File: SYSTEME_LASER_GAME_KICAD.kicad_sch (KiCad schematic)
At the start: 4 parts, among them U1 nRF9151-LAXX, U2 LDO_3.3V_0.1A

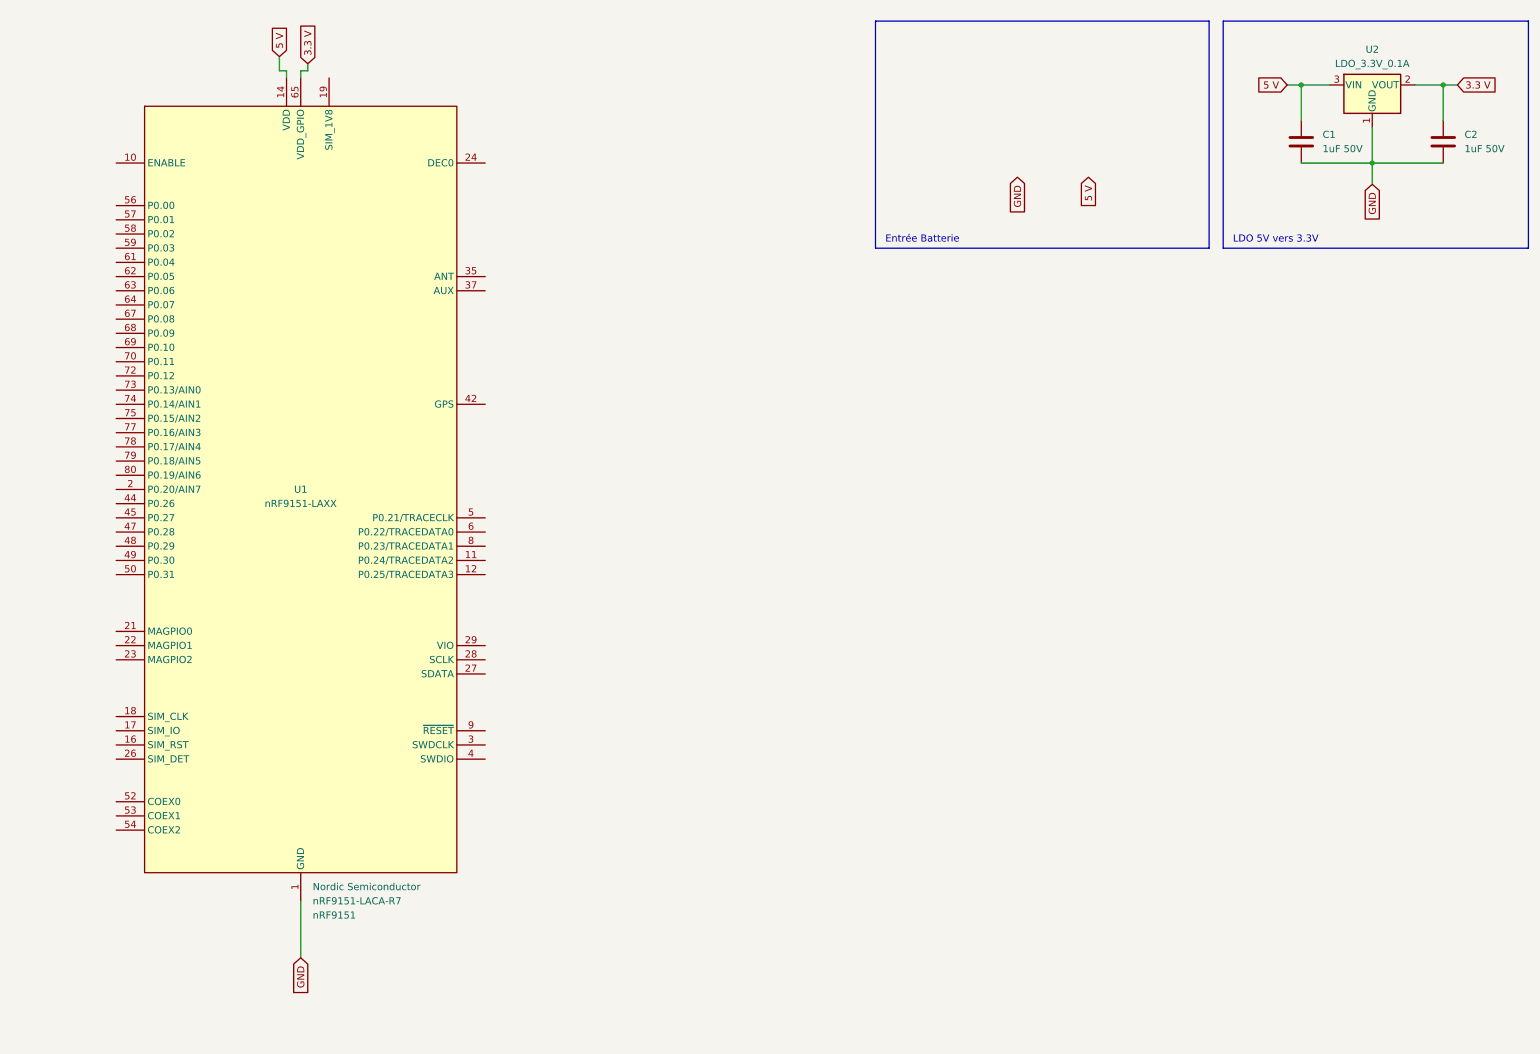
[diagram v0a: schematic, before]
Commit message: réalisation des tests, et fixation des nombres de composants sur le KiCad
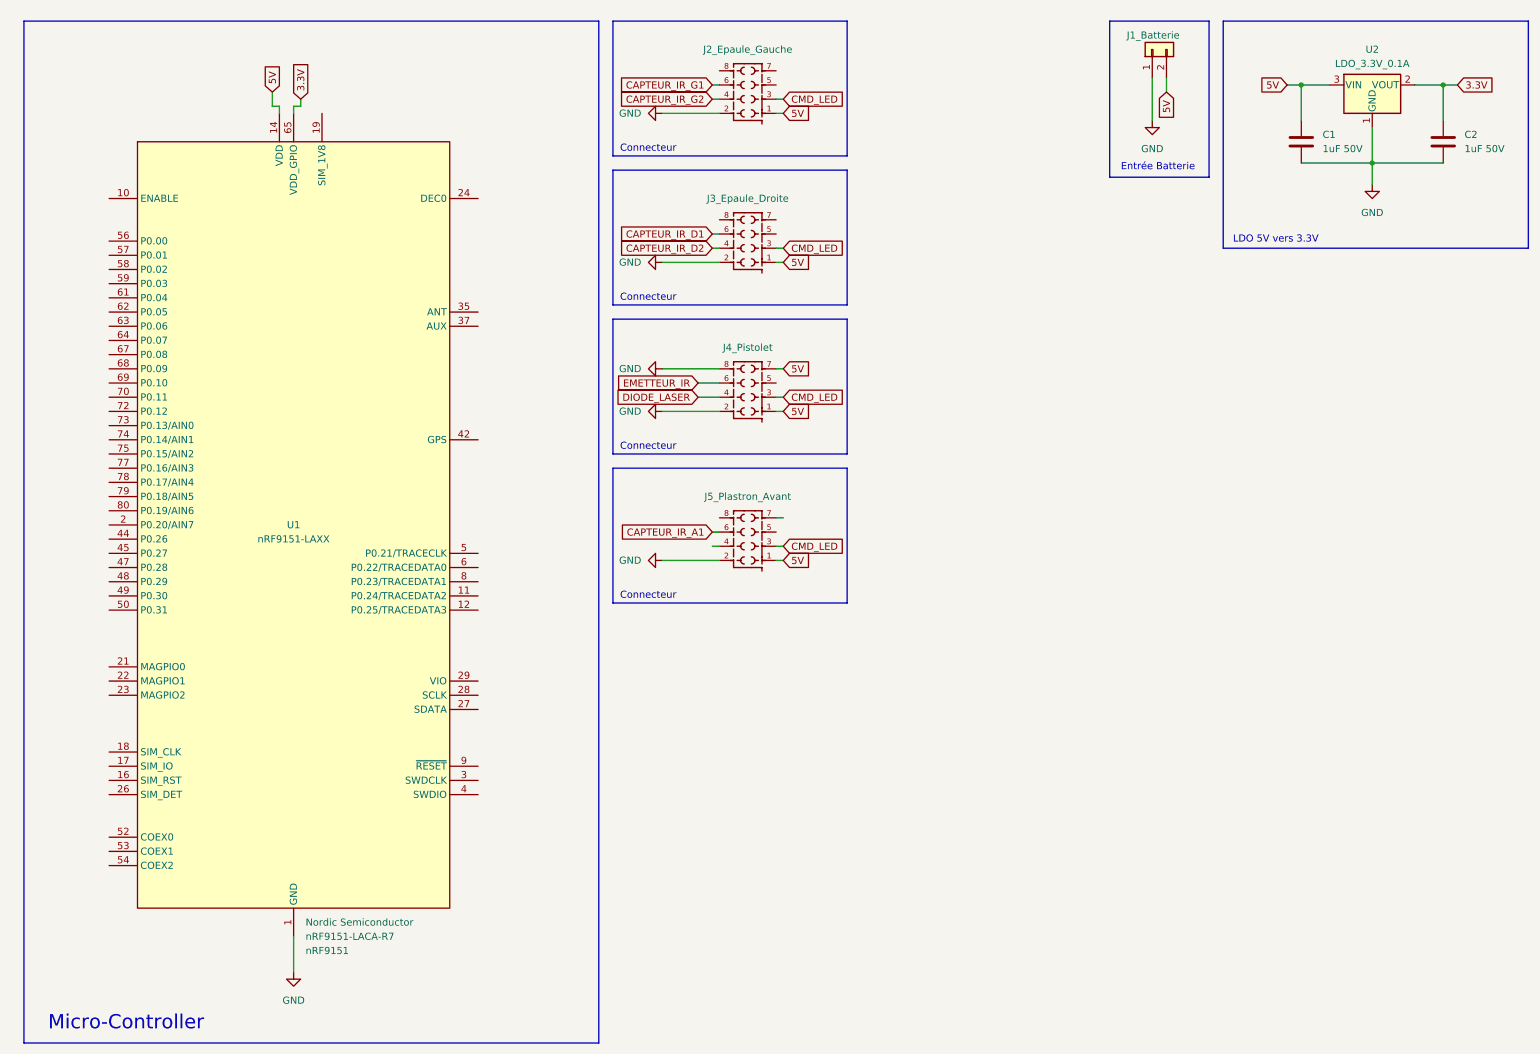
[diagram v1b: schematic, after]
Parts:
- added J1_Batterie: EMB_P3.81_1x02_VERTICAL, codium_Connectors:Conn_THT_3.81_2x1_Vertical, symbol codium_Connectors:EMB_P3.81_1x02_VERTICAL
- added J2_Epaule_Gauche, J3_Epaule_Droite, J4_Pistolet, J5_Plastron_Avant: PinSocket_2x04_P2.54mm_Horizontal_SMD, codium_Connectors:PinSocket_2x04_P2.54mm_Horizontal_SMD, symbol codium_Connectors:PinSocket_2x04_P2.54mm_Horizontal_SMD
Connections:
- net GND: now also J1_Batterie.1 (Pin_1), J2_Epaule_Gauche.2, J3_Epaule_Droite.2, J4_Pistolet.2, J4_Pistolet.8, J5_Plastron_Avant.2
- net 3.3 V renamed 3.3V
- net 5 V renamed 5V
- net 5V: now also J1_Batterie.2 (Pin_2), J2_Epaule_Gauche.1, J3_Epaule_Droite.1, J4_Pistolet.1, J4_Pistolet.7, J5_Plastron_Avant.1
- new net CAPTEUR_IR_A1: J5_Plastron_Avant.6
- new net CAPTEUR_IR_D1: J3_Epaule_Droite.6
- new net CAPTEUR_IR_D2: J3_Epaule_Droite.4
- new net CAPTEUR_IR_G1: J2_Epaule_Gauche.6
- new net CAPTEUR_IR_G2: J2_Epaule_Gauche.4
- new net CMD_LED: J2_Epaule_Gauche.3, J3_Epaule_Droite.3, J4_Pistolet.3, J5_Plastron_Avant.3
- new net DIODE_LASER: J4_Pistolet.4
- new net EMETTEUR_IR: J4_Pistolet.6
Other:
- note added: "Connecteur"
- note added: "Micro-Controller"
- moved on the sheet: U1

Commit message: Finalisation test IR et amélioration CAO sur KiCad
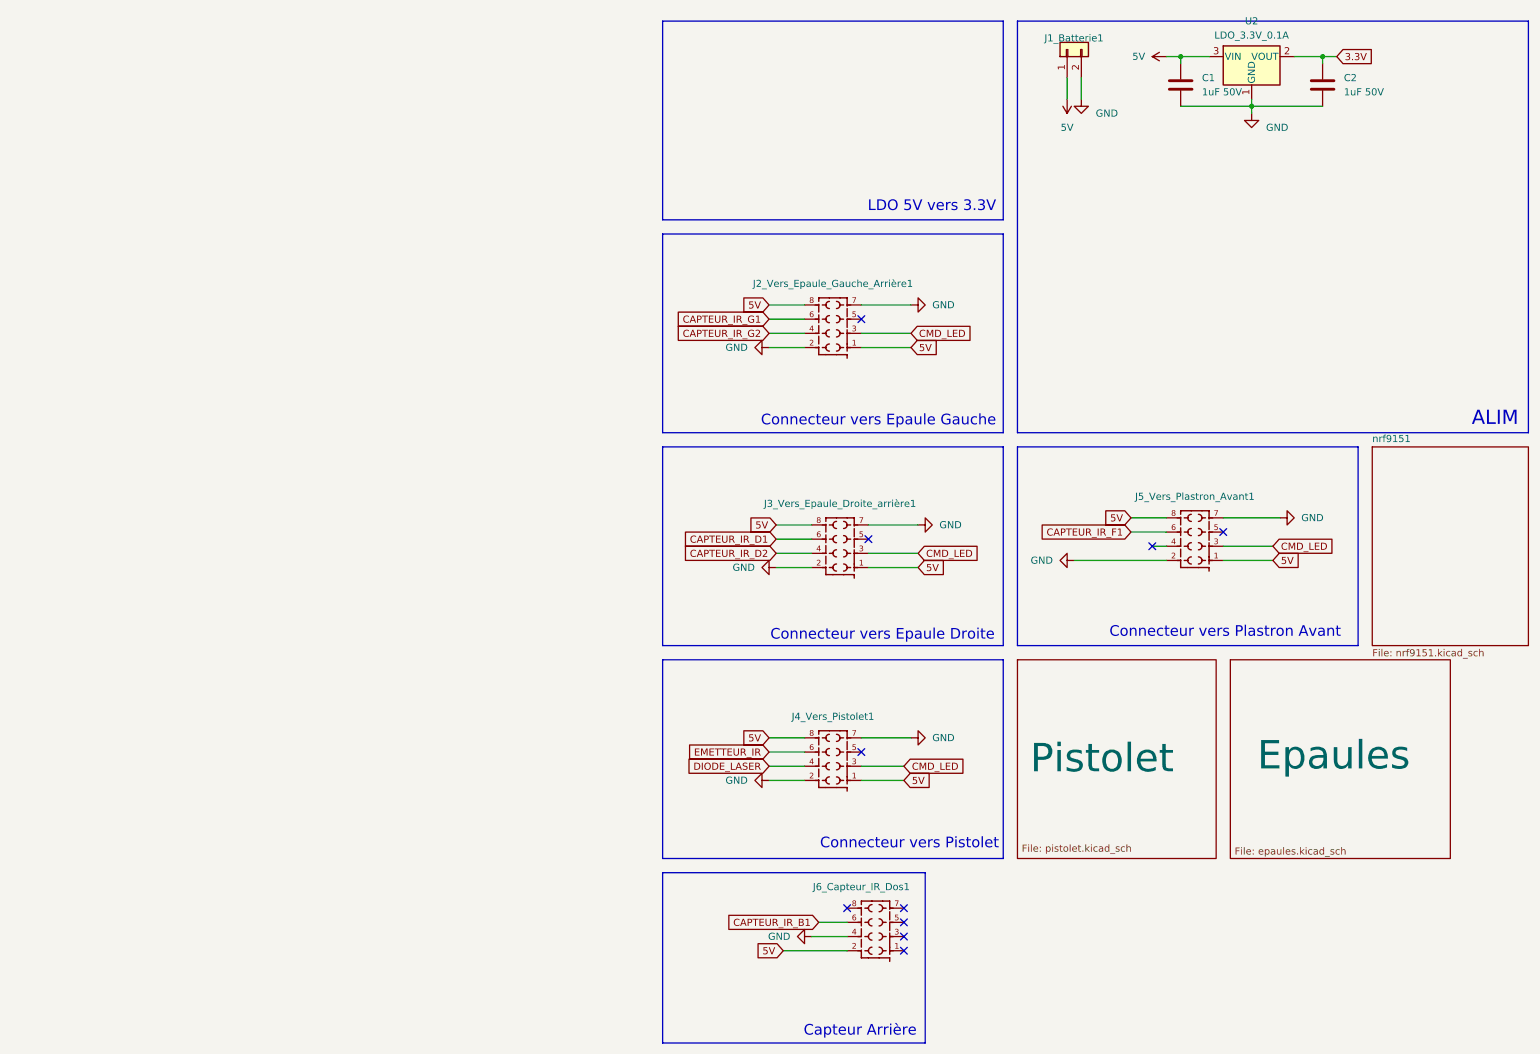
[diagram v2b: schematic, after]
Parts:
- removed J1_Batterie: EMB_P3.81_1x02_VERTICAL, codium_Connectors:Conn_THT_3.81_2x1_Vertical, symbol codium_Connectors:EMB_P3.81_1x02_VERTICAL
- removed U1: nRF9151-LAXX, codium_LGA_BGA:LGA_9151_12.1x11.1mm, symbol codium_IC:nRF9151-LAXX
- added J1_Batterie1: EMB_P3.81_1x02_VERTICAL, codium_Connectors:Conn_THT_3.81_2x1_Vertical, symbol codium_Connectors:EMB_P3.81_1x02_VERTICAL
- added J6_Capteur_IR_Dos1: PinSocket_2x04_P2.54mm_Horizontal_SMD, codium_Connectors:PinSocket_2x04_P2.54mm_Horizontal_SMD, symbol codium_Connectors:PinSocket_2x04_P2.54mm_Horizontal_SMD
- renumbered J2_Epaule_Gauche to J2_Vers_Epaule_Gauche_Arrière1, J3_Epaule_Droite to J3_Vers_Epaule_Droite_arrière1, J4_Pistolet to J4_Vers_Pistolet1, J5_Plastron_Avant to J5_Vers_Plastron_Avant1
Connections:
- net 5V: now also J2_Vers_Epaule_Gauche_Arrière1.8, J3_Vers_Epaule_Droite_arrière1.8, J4_Vers_Pistolet1.8, J5_Vers_Plastron_Avant1.8, J1_Batterie1.1 (Pin_1), J6_Capteur_IR_Dos1.2; no longer J4_Vers_Pistolet1.7
- net GND: now also J2_Vers_Epaule_Gauche_Arrière1.7, J3_Vers_Epaule_Droite_arrière1.7, J4_Vers_Pistolet1.7, J5_Vers_Plastron_Avant1.7, J1_Batterie1.2 (Pin_2), J6_Capteur_IR_Dos1.4; no longer J4_Vers_Pistolet1.8
- net CAPTEUR_IR_A1 renamed CAPTEUR_IR_F1
- new net CAPTEUR_IR_B1: J6_Capteur_IR_Dos1.6
- no-connect marks 0 -> 10
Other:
- added sheet Epaules (epaules.kicad_sch)
- added sheet Pistolet (pistolet.kicad_sch)
- added sheet nrf9151 (nrf9151.kicad_sch)
- note added: "ALIM"
- note added: "Capteur Arrière"
- note added: "Connecteur vers Epaule Droite"
- note added: "Connecteur vers Epaule Gauche"
- note added: "Connecteur vers Pistolet"
- note added: "Connecteur vers Plastron Avant"
- note removed: "Connecteur"
- note removed: "Entrée Batterie"
- note removed: "Micro-Controller"
- moved on the sheet: C1, C2, J2_Vers_Epaule_Gauche_Arrière1, J3_Vers_Epaule_Droite_arrière1, J4_Vers_Pistolet1, J5_Vers_Plastron_Avant1, U2
